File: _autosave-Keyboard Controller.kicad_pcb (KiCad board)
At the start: 2 copper layers, 76.2 x 101.6 mm, 52 parts, among them SW1 SW_Push, SW2 SW_Push, SW3 SW_Push, SW4 SW_Push, SW5 SW_Push, SW6 SW_Push, SW7 SW_Push, SW8 SW_Push, SW9 SW_Push, U1 Teensy-3.2

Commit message: All placements finalized
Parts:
- moved R5 19.7 mm to (112.4, 78.1)
- moved R3 18.5 mm to (137.8, 47.6)
- moved R2 11.8 mm to (112.4, 47.6)
- moved R26 10.2 mm to (136.5, 124.5)
- moved R16 8.54 mm to (158.1, 63.5)
- moved R7 7.73 mm to (160.0, 78.7)
- moved R4 7.24 mm to (160.7, 47.6)
- moved R12 6.98 mm to (111.1, 63.5)
- moved R27 6.38 mm to (159.4, 125.1)
- moved R17 4.44 mm to (111.1, 88.9), turned to 180 degrees
- moved R18 3.86 mm to (111.1, 92.7), turned to 0 degrees
- moved R28 3.81 mm to (159.4, 118.7), turned to 180 degrees
- moved R14 2.01 mm to (136.5, 62.2)
- moved R13 1.91 mm to (136.5, 57.8), turned to 180 degrees
- moved R6 1.80 mm to (137.8, 83.8)
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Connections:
- net Net-(SW1-Pad1) renamed /SW1
- net Net-(SW2-Pad1) renamed /SW2
- net Net-(SW3-Pad1) renamed /SW3
- net Net-(SW4-Pad1) renamed /SW4
- net Net-(SW5-Pad1) renamed /SW5
- net Net-(SW6-Pad1) renamed /SW6
- net Net-(SW7-Pad1) renamed /SW7
- net Net-(SW8-Pad1) renamed /SW8
- net Net-(SW9-Pad1) renamed /SW9
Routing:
- net GND: track 0.00 -> 225.3 mm
- net +3V3: track 0.00 -> 154.7 mm
- net /SW6: track 0.00 -> 64.8 mm
- net /SW5: track 0.00 -> 47.7 mm
- net /SW4: track 0.00 -> 46.4 mm
- net /SW3: track 0.00 -> 42.9 mm, vias 0 -> 1
- net /SW1: track 0.00 -> 26.5 mm
- net /SW2: track 0.00 -> 7.51 mm
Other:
- net class Default: clearance 0.2 -> 0.1524; trace_width 0.25 -> 0.254; via_dia 0.6 -> 0.6858; via_drill 0.4 -> 0.3302
- rule trace_clearance: 0.2 -> 0.1524
- rule trace_min: 0.2 -> 0.1524
- rule via_min_drill: 0.3 -> 0.3302
- rule via_min_size: 0.4 -> 0.6858

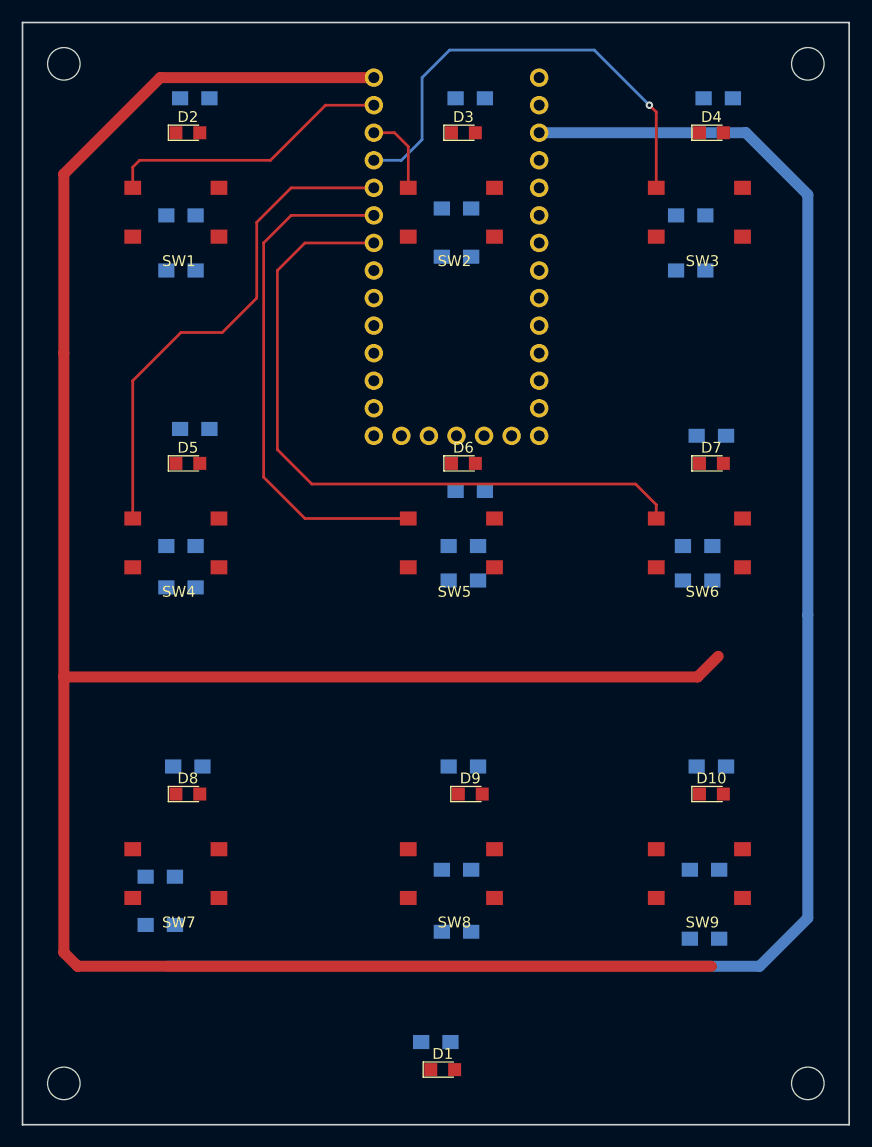
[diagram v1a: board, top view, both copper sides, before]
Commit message: Changed pinout for easier layout
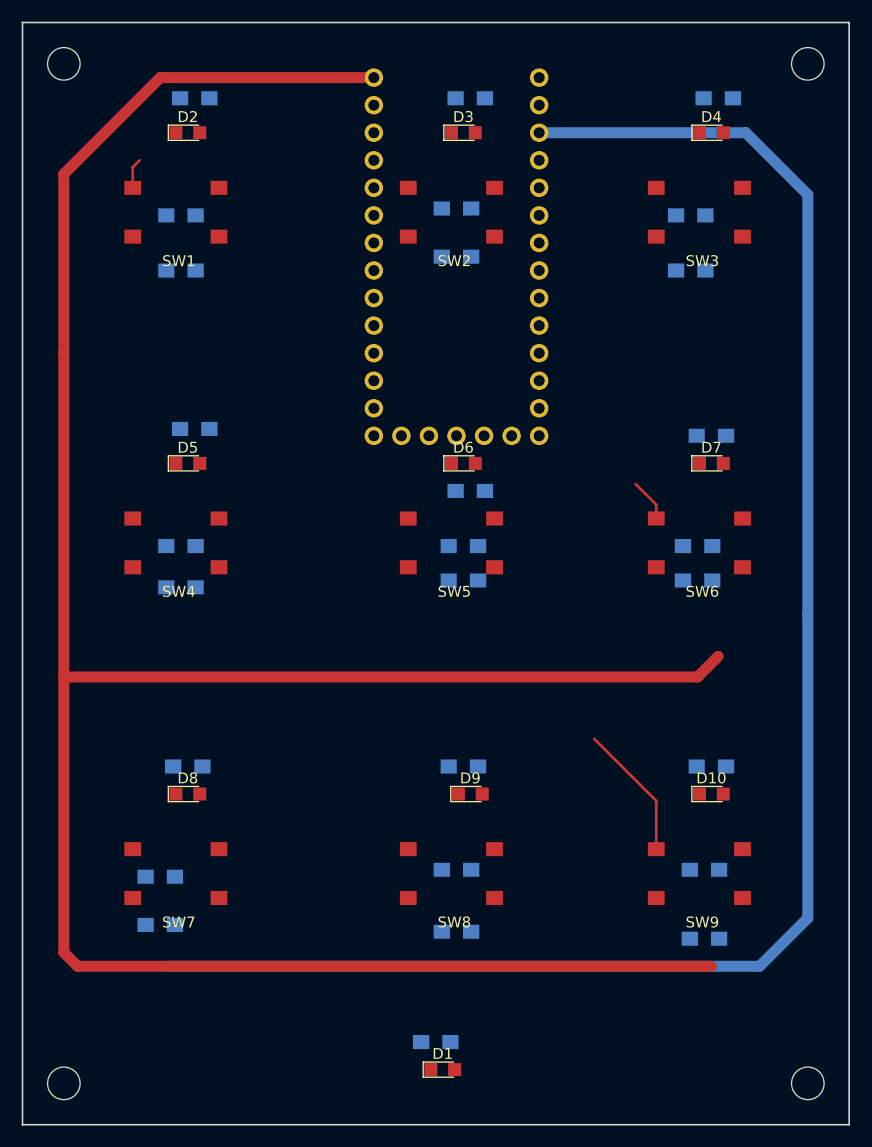
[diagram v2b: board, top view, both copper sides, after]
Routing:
- net /SW6: track 64.8 -> 3.96 mm
- net /SW5: track 47.7 -> 0.00 mm
- net /SW4: track 46.4 -> 0.00 mm
- net /SW3: track 42.9 -> 0.00 mm, vias 1 -> 0
- net /SW1: track 26.5 -> 2.80 mm
- net /SW9: track 0.00 -> 12.5 mm
- net /SW2: track 7.51 -> 0.00 mm
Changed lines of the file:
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@@
   (general
     (links 75)
-    (no_connects 69)
-    (area 96.444999 40.564999 172.795001 142.315001)
+    (no_connects 75)
+    (area 92.963314 39.5226 176.276686 143.4574)
     (thickness 1.6)
     (drawings 4)
-    (tracks 51)
+    (tracks 21)
     (zones 0)
     (modules 52)
@@
     (aux_axis_origin 0 0)
     (grid_origin 100.33 52.07)
-    (visible_elements FFFEF77F)
+    (visible_elements 7FFFFFFF)
     (pcbplotparams
       (layerselection 0x00030_80000001)
@@
   (segment (start 100.33 100.965) (end 100.33 126.365) (width 1.016) (layer F.Cu) (net 12))
   (segment (start 109.22 45.72) (end 100.33 54.61) (width 1.016) (layer F.Cu) (net 12))
-  (segment (start 128.905 48.26) (end 124.46 48.26) (width 0.254) (layer F.Cu) (net 44) (status 400000))
-  (segment (start 106.68 53.975) (end 106.68 55.88) (width 0.254) (layer F.Cu) (net 44) (status 800000))
+  (segment (start 106.68 53.975) (end 106.68 55.88) (width 0.254) (layer F.Cu) (net 44))
   (segment (start 107.315 53.34) (end 106.68 53.975) (width 0.254) (layer F.Cu) (net 44))
-  (segment (start 119.38 53.34) (end 107.315 53.34) (width 0.254) (layer F.Cu) (net 44))
-  (segment (start 124.46 48.26) (end 119.38 53.34) (width 0.254) (layer F.Cu) (net 44))
-  (segment (start 128.905 50.8) (end 130.81 50.8) (width 0.254) (layer F.Cu) (net 45) (status 400000))
-  (segment (start 132.08 52.07) (end 132.08 55.88) (width 0.254) (layer F.Cu) (net 45) (status 800000))
-  (segment (start 130.81 50.8) (end 132.08 52.07) (width 0.254) (layer F.Cu) (net 45))
-  (segment (start 128.905 53.34) (end 131.445 53.34) (width 0.254) (layer B.Cu) (net 46) (status 400000))
-  (segment (start 154.94 48.895) (end 154.94 55.88) (width 0.254) (layer F.Cu) (net 46) (status 800000))
-  (segment (start 154.305 48.26) (end 154.94 48.895) (width 0.254) (layer F.Cu) (net 46))
-  (via (at 154.305 48.26) (size 0.6858) (drill 0.3302) (layers F.Cu B.Cu) (net 46))
-  (segment (start 149.225 43.18) (end 154.305 48.26) (width 0.254) (layer B.Cu) (net 46))
-  (segment (start 135.89 43.18) (end 149.225 43.18) (width 0.254) (layer B.Cu) (net 46))
-  (segment (start 133.35 45.72) (end 135.89 43.18) (width 0.254) (layer B.Cu) (net 46))
-  (segment (start 133.35 51.435) (end 133.35 45.72) (width 0.254) (layer B.Cu) (net 46))
-  (segment (start 131.445 53.34) (end 133.35 51.435) (width 0.254) (layer B.Cu) (net 46))
-  (segment (start 128.905 55.88) (end 121.285 55.88) (width 0.254) (layer F.Cu) (net 47) (status 400000))
-  (segment (start 106.68 73.66) (end 106.68 86.36) (width 0.254) (layer F.Cu) (net 47) (status 800000))
-  (segment (start 111.125 69.215) (end 106.68 73.66) (width 0.254) (layer F.Cu) (net 47))
-  (segment (start 114.935 69.215) (end 111.125 69.215) (width 0.254) (layer F.Cu) (net 47))
-  (segment (start 118.11 66.04) (end 114.935 69.215) (width 0.254) (layer F.Cu) (net 47))
-  (segment (start 118.11 59.055) (end 118.11 66.04) (width 0.254) (layer F.Cu) (net 47))
-  (segment (start 121.285 55.88) (end 118.11 59.055) (width 0.254) (layer F.Cu) (net 47))
-  (segment (start 128.905 58.42) (end 121.285 58.42) (width 0.254) (layer F.Cu) (net 48) (status 400000))
-  (segment (start 122.555 86.36) (end 132.08 86.36) (width 0.254) (layer F.Cu) (net 48) (status 800000))
-  (segment (start 118.745 82.55) (end 122.555 86.36) (width 0.254) (layer F.Cu) (net 48))
-  (segment (start 118.745 60.96) (end 118.745 82.55) (width 0.254) (layer F.Cu) (net 48))
-  (segment (start 121.285 58.42) (end 118.745 60.96) (width 0.254) (layer F.Cu) (net 48))
-  (segment (start 128.905 60.96) (end 122.555 60.96) (width 0.254) (layer F.Cu) (net 49) (status 400000))
-  (segment (start 154.94 85.09) (end 154.94 86.36) (width 0.254) (layer F.Cu) (net 49) (status 800000))
+  (segment (start 154.94 85.09) (end 154.94 86.36) (width 0.254) (layer F.Cu) (net 49))
   (segment (start 153.035 83.185) (end 154.94 85.09) (width 0.254) (layer F.Cu) (net 49))
-  (segment (start 123.19 83.185) (end 153.035 83.185) (width 0.254) (layer F.Cu) (net 49))
-  (segment (start 120.015 80.01) (end 123.19 83.185) (width 0.254) (layer F.Cu) (net 49))
-  (segment (start 120.015 63.5) (end 120.015 80.01) (width 0.254) (layer F.Cu) (net 49))
-  (segment (start 122.555 60.96) (end 120.015 63.5) (width 0.254) (layer F.Cu) (net 49))
+  (segment (start 154.94 112.395) (end 154.94 116.84) (width 0.254) (layer F.Cu) (net 52))
+  (segment (start 149.225 106.68) (end 154.94 112.395) (width 0.254) (layer F.Cu) (net 52))
 )
